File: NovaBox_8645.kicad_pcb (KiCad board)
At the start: 2 copper layers, 90 x 29 mm, 68 parts, among them P1 MH, P3 MH, P4 MH, P5 MH, Q1 MMBT3904_l, Q2 8205S, SW2 NEXT, SW3 PREV, SW4 PP, SW5 VOL+, SW6 VOL-, SW7 ON/OFF, U1 CSR8645_MODULE, U2 DW01, U3 PAM8304, U4 PAM8304, U5 MCP6004_l, U6 CSR_DebugSmall

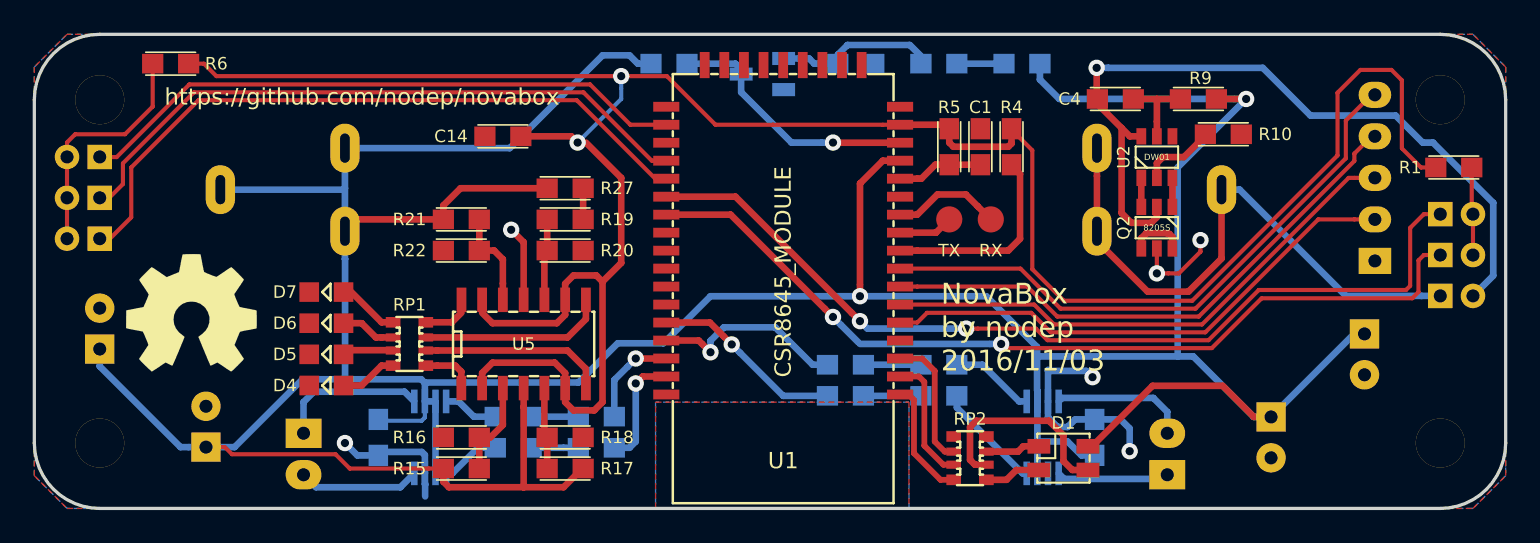
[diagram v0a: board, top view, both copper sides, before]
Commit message: tweaked pad sizes
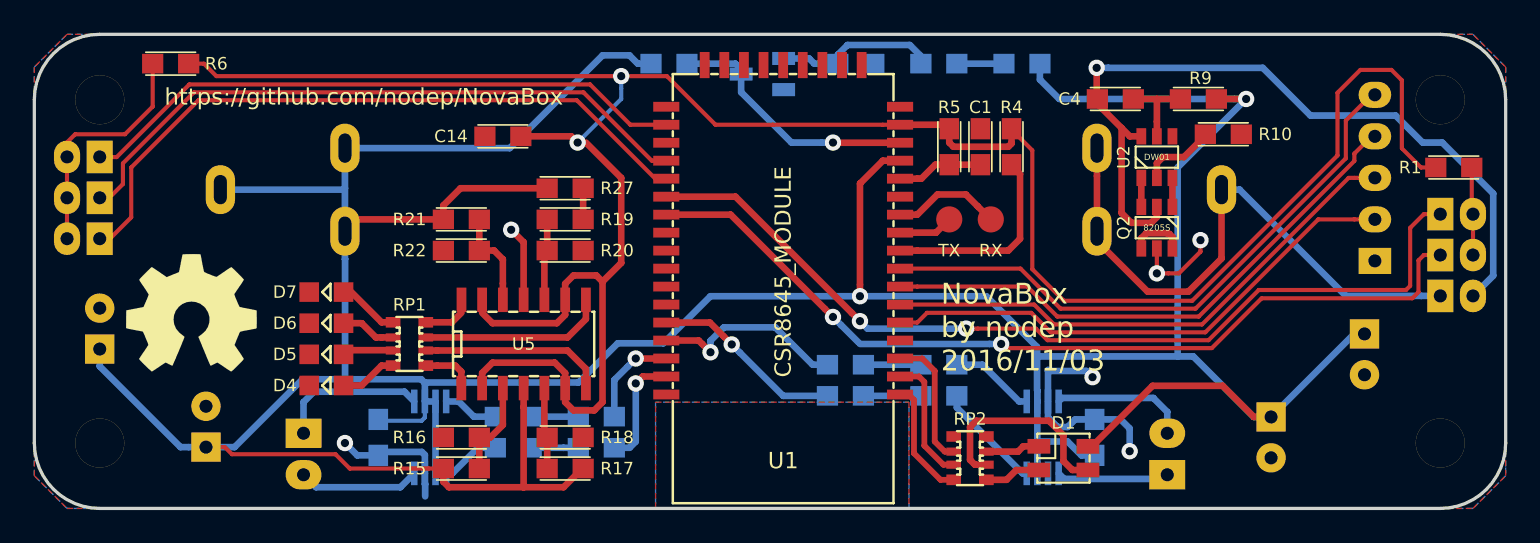
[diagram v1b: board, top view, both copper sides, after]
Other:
- board text added: "https://github.com/nodep/NovaBox"
- board text removed: "https://github.com/nodep/novabox"

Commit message: sent gerbers to fab
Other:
- board text added: "NovaBox by čika c 2016/11/06"
- board text removed: "NovaBox by nodep 2016/11/03"
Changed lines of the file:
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@@
   (gr_arc (start 49 161) (end 49 165) (angle 90) (layer Edge.Cuts) (width 0.2))
   (gr_arc (start 49 140) (end 45 140) (angle 90) (layer Edge.Cuts) (width 0.2))
-  (gr_text "NovaBox\nby nodep\n2016/11/03" (at 100.457 153.924) (layer F.SilkS)
+  (gr_text "NovaBox\nby čika c\n2016/11/06" (at 100.457 153.924) (layer F.SilkS)
     (effects (font (thickness 0.254)) (justify left))
   )

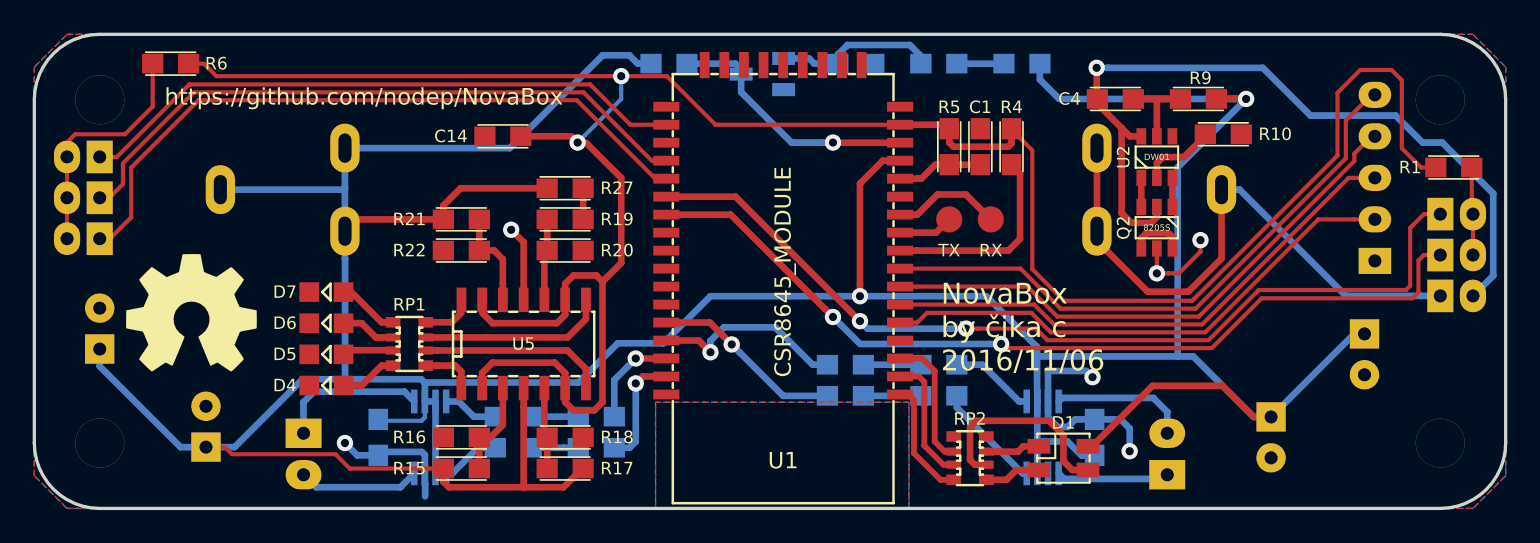
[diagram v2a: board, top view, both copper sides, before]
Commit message: fixed some 3D models on CSR8645
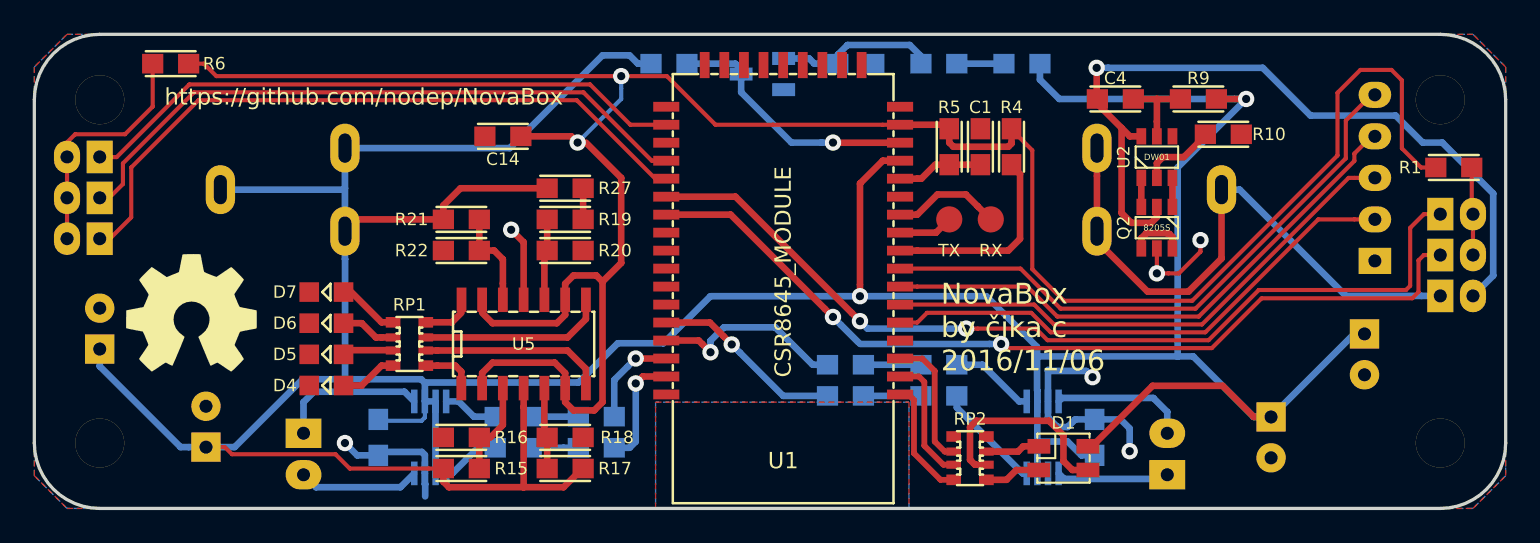
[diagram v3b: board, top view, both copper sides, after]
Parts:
- C1, C10, C11, C12, C13, C14, C2, C4, C8, C9: footprint NovaBox:SMD0805 -> NovaBox:C_0805
- R1, R10, R11, R12, R13, R14, R15, R16, R17, R18, R19, R2, R20, R21, R22, R27, R3, R4, R5, R6, R7, R9: footprint NovaBox:SMD0805 -> NovaBox:R_0805

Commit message: reverted the PWER_E (R3 and R7) to their suggested values
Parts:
- R3: value 10K -> 1K
- R7: value 100K -> 10K
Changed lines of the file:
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@@
       (effects (font (size 0.762 0.762) (thickness 0.127)) (justify mirror))
     )
-    (fp_text value 10K (at 0 0 270) (layer Dwgs.User) hide
+    (fp_text value 1K (at 0 0 270) (layer Dwgs.User) hide
       (effects (font (size 0.127 0.127) (thickness 0.0254)))
     )
@@
       (effects (font (size 0.762 0.762) (thickness 0.127)) (justify mirror))
     )
-    (fp_text value 100K (at 0 0 450) (layer Dwgs.User) hide
+    (fp_text value 10K (at 0 0 450) (layer Dwgs.User) hide
       (effects (font (size 0.127 0.127) (thickness 0.0254)))
     )
